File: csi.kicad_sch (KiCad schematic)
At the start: 65 parts, among them J1 200528-0150, J12 200528-0150, J6 200528-0150, J9 200528-0150, U24 AP22615A, U25 AP22615A, U26 PI4MSD5V9548AZDEX, U3 AP22615A, U31 NTS0102, U32 NTS0102, U7 AP22615A

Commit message: v2.0 Schematic updates
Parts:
- added R182, R183, R184, R185: 0R, Resistor_SMD:R_0603_1608Metric, symbol Device:R_Small
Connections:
- net +3V3: now also R182.1, R183.1, R184.1, R185.1
- net 3V3_CAM0: now also R182.2
- net 3V3_CAM1: now also R184.2
- net 3V3_CAM2: now also R183.2
- net 3V3_CAM3: now also R185.2
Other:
- company: Argus-1 Cubesat -> Carnegie Mellon University
- title: Jetson Carrier Board -> Argus Carrierboard
- moved on the sheet: C39, C43, C47, C79, D10, D11, D12, D13, R10, R180, R2, R3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

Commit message: v2.0 Layout completed. Exported BOM and STEP files
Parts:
- J1, J12, J6, J9: footprint Connector_FFC-FPC:Molex_200528-0150_1x15-1MP_P1.00mm_Horizontal -> JetsonCarrier:CON_522071560_MOL
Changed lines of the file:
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@@
 (kicad_sch
-	(version 20231120)
+	(version 20250114)
 	(generator "eeschema")
-	(generator_version "8.0")
+	(generator_version "9.0")
 	(paper "A3")
 	(title_block
@@
 		(comment 2 "N. Khera")
 	)
+	(text "Power switches"
+		(exclude_from_sim no)
+		(at 119.38 189.865 0)
+		(effects
+			(font
+				(size 4 4)
+				(thickness 0.8)
+				(bold yes)
+			)
+			(justify left bottom)
+		)
+	)
+	(text "CSI connectors"
+		(exclude_from_sim no)
+		(at 285.496 22.606 0)
+		(effects
+			(font
+				(size 4 4)
+				(thickness 0.8)
+				(bold yes)
+			)
+			(justify left bottom)
+		)
+	)
+	(text "I2C Mux"
+		(exclude_from_sim no)
+		(at 89.408 22.606 0)
+		(effects
+			(font
+				(size 4 4)
+				(thickness 0.8)
+				(bold yes)
+			)
+			(justify left bottom)
+		)
+	)
+	(text "ALL SWITCHES\n1.5A CURRENT LIMIT"
+		(exclude_from_sim no)
+		(at 120.65 195.326 0)
+		(effects
+			(font
+				(size 1.27 1.27)
+			)
+			(justify left bottom)
+		)
+	)
+	(text "Level shifters"
+		(exclude_from_sim no)
+		(at 331.47 187.96 0)
+		(effects
+			(font
+				(size 4 4)
+				(thickness 0.8)
+				(bold yes)
+			)
+			(justify left bottom)
+		)
+	)
 	(junction
 		(at 93.98 119.38)
@@
 		)
 	)
-	(text "Power switches"
-		(exclude_from_sim no)
-		(at 119.38 189.865 0)
-		(effects
-			(font
-				(size 4 4)
-				(thickness 0.8)
-				(bold yes)
-			)
-			(justify left bottom)
-		)
-	)
-	(text "CSI connectors"
-		(exclude_from_sim no)
-		(at 285.496 22.606 0)
-		(effects
-			(font
-				(size 4 4)
-				(thickness 0.8)
-				(bold yes)
-			)
-			(justify left bottom)
-		)
-	)
-	(text "I2C Mux"
-		(exclude_from_sim no)
-		(at 89.408 22.606 0)
-		(effects
-			(font
-				(size 4 4)
-				(thickness 0.8)
-				(bold yes)
-			)
-			(justify left bottom)
-		)
-	)
-	(text "ALL SWITCHES\n1.5A CURRENT LIMIT"
-		(exclude_from_sim no)
-		(at 120.65 195.326 0)
-		(effects
-			(font
-				(size 1.27 1.27)
-			)
-			(justify left bottom)
-		)
-	)
-	(text "Level shifters"
-		(exclude_from_sim no)
-		(at 331.47 187.96 0)
-		(effects
-			(font
-				(size 4 4)
-				(thickness 0.8)
-				(bold yes)
-			)
-			(justify left bottom)
-		)
-	)
 	(label "SDA_CAM0"
 		(at 127 63.5 180)
@@
 			)
 		)
-		(property "Footprint" "Connector_FFC-FPC:Molex_200528-0150_1x15-1MP_P1.00mm_Horizontal"
+		(property "Footprint" "JetsonCarrier:CON_522071560_MOL"
 			(at 293.37 134.62 0)
 			(effects
@@
 			)
 		)
-		(property "Footprint" "Connector_FFC-FPC:Molex_200528-0150_1x15-1MP_P1.00mm_Horizontal"
+		(property "Footprint" "JetsonCarrier:CON_522071560_MOL"
 			(at 365.76 134.62 0)
 			(effects
@@
 			)
 		)
-		(property "Footprint" "Connector_FFC-FPC:Molex_200528-0150_1x15-1MP_P1.00mm_Horizontal"
+		(property "Footprint" "JetsonCarrier:CON_522071560_MOL"
 			(at 365.76 64.77 0)
 			(effects
@@
 			)
 		)
-		(property "Footprint" "Connector_FFC-FPC:Molex_200528-0150_1x15-1MP_P1.00mm_Horizontal"
+		(property "Footprint" "JetsonCarrier:CON_522071560_MOL"
 			(at 293.37 64.77 0)
 			(effects

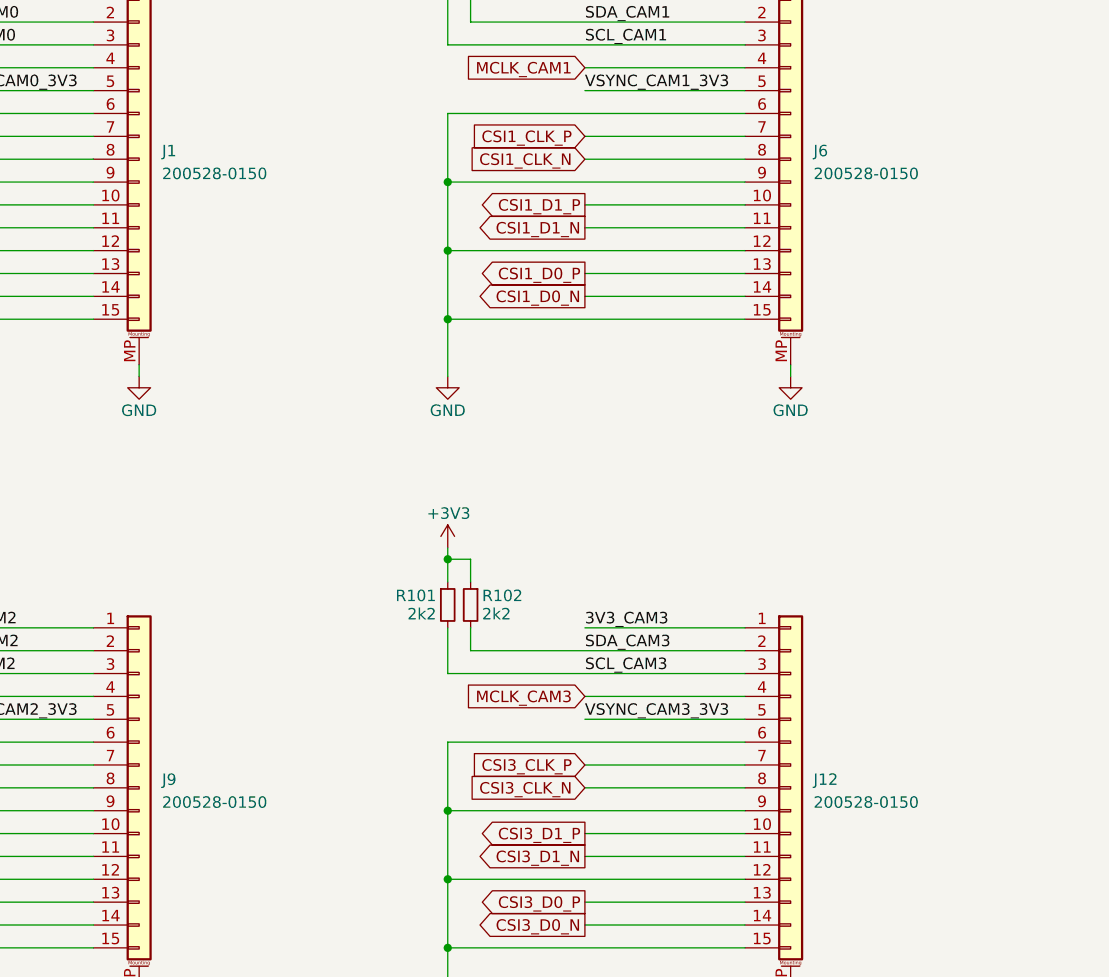
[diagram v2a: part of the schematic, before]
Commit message: Fix connector name
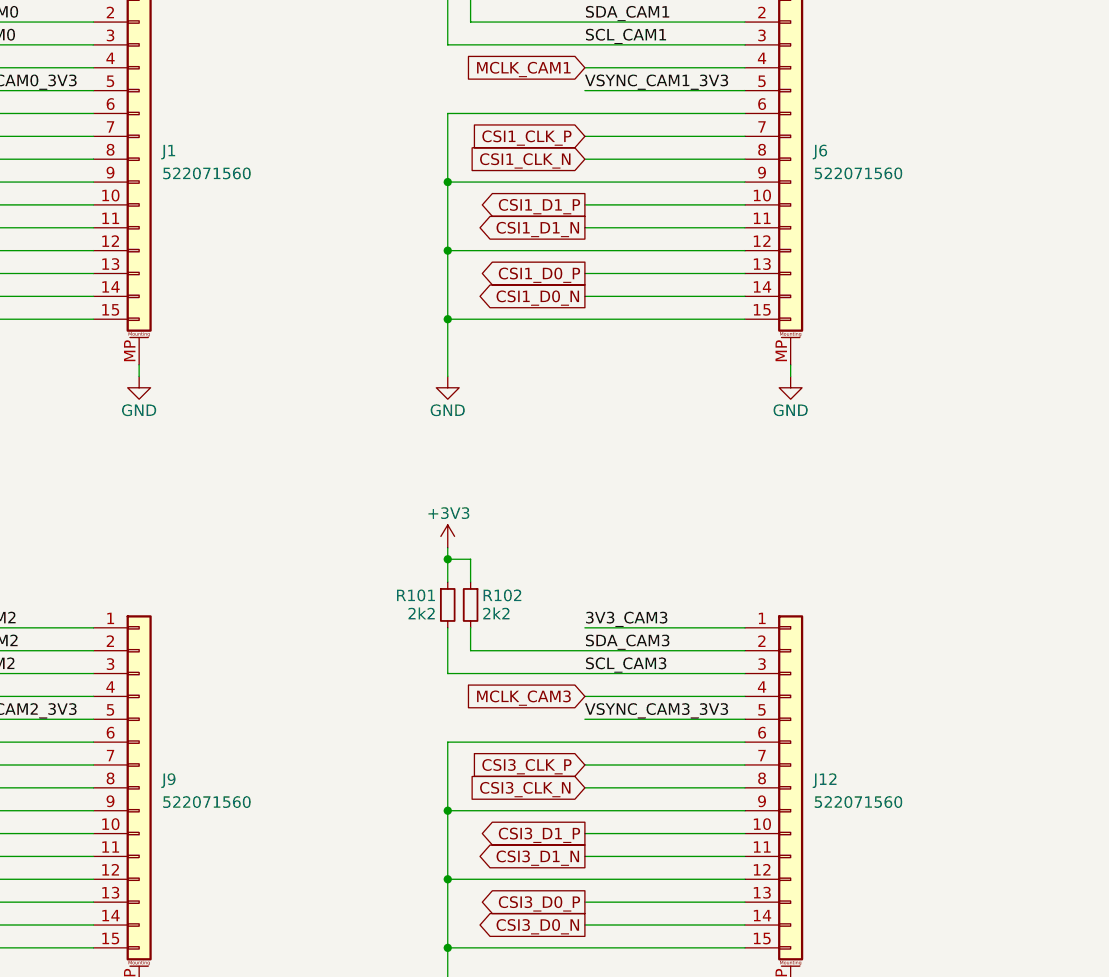
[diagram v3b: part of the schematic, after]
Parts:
- J1, J12, J6, J9: value 200528-0150 -> 522071560
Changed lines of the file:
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@@
 			)
 		)
-		(property "Value" "200528-0150"
+		(property "Value" "522071560"
 			(at 295.91 136.2455 0)
 			(effects
@@
 			)
 		)
-		(property "Value" "200528-0150"
+		(property "Value" "522071560"
 			(at 368.3 136.2455 0)
 			(effects
@@
 			)
 		)
-		(property "Value" "200528-0150"
+		(property "Value" "522071560"
 			(at 368.3 66.3955 0)
 			(effects
@@
 			)
 		)
-		(property "Value" "200528-0150"
+		(property "Value" "522071560"
 			(at 295.91 66.3955 0)
 			(effects

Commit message: v2.1 Updates
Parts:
- C100, C101, C39, C43, C47, C79, C89, C96, C97: Author Antmicro -> (none); Dielectric X5R -> (none); License Apache-2.0 -> (none); MPN GRM155R61H104KE14D -> C307348; Val 100n -> (none); Voltage 50V -> (none)
- D10, D11, D12, D13: Author Antmicro -> (none); License Apache-2.0 -> (none); MPN LTST-C190GKT -> C2909774; Manufacturer Lite-On -> (none); Public False -> (none)
- R10, R2, R51, R6: Author Antmicro -> (none); License Apache-2.0 -> (none); MPN CR0402-FX-1003GLF -> C237792; Manufacturer Bourns -> (none); Tolerance 1% -> (none); Val 100k -> (none)
- R101, R102, R26, R36, R48, R54, R55, R63: MPN (none) -> C2076947
- R142, R35, R53: Author Antmicro -> (none); Current 1A -> (none); License Apache-2.0 -> (none); MPN ERJ2GE0R00X -> C190119; Manufacturer Panasonic -> (none); Val 0R -> (none)
- R144, R3, R64, R66, R67: Author Antmicro -> (none); License Apache-2.0 -> (none); MPN CR0402-FX-1002GLF -> C2479067; Manufacturer Bourns -> (none); Tolerance 1% -> (none); Val 10k -> (none)
- R180, R182, R183, R184, R185, R34, R40, R50, R9, TP13, TP14, TP17, TP18, TP19, TP20, TP8, TP9: now left out of the parts list
- R7, R8, R85, R86, R87, R88, R89, R90: Author Antmicro -> (none); License Apache-2.0 -> (none); MPN CR0402-FX-4701GLF -> C844931; Manufacturer Bourns -> (none); Tolerance 1% -> (none); Val 4k7 -> (none)
- U24, U25, U3, U7: Author Antmicro -> (none); License Apache-2.0 -> (none); MPN AP22615AWU-7 -> C2680357; Manufacturer Diodes Incorporated -> (none)
